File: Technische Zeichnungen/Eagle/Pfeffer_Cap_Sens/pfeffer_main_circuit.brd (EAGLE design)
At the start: 38 x 50 mm, 20 parts

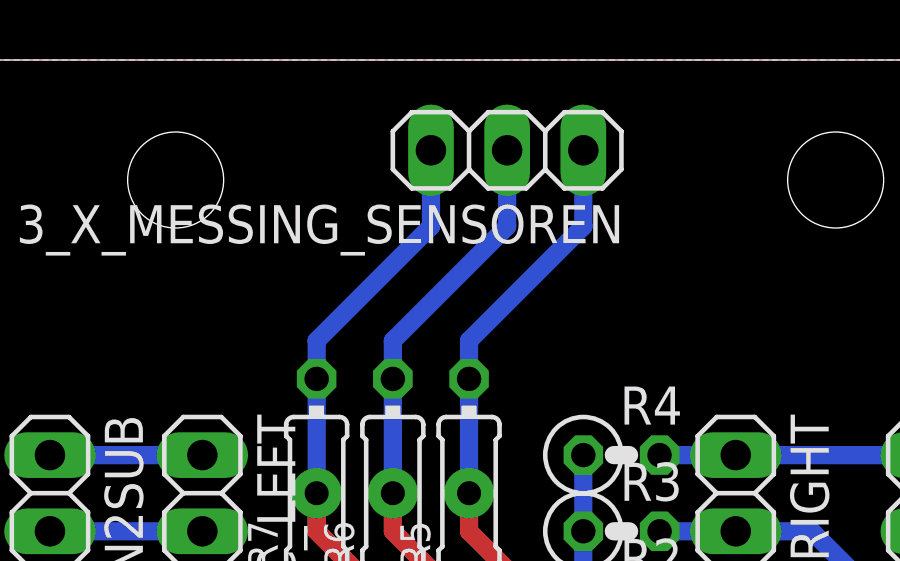
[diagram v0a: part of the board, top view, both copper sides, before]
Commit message: added ribbon testing, firmware and applied it to the new firmware, added a new tech. drawing, added new PCB layouts
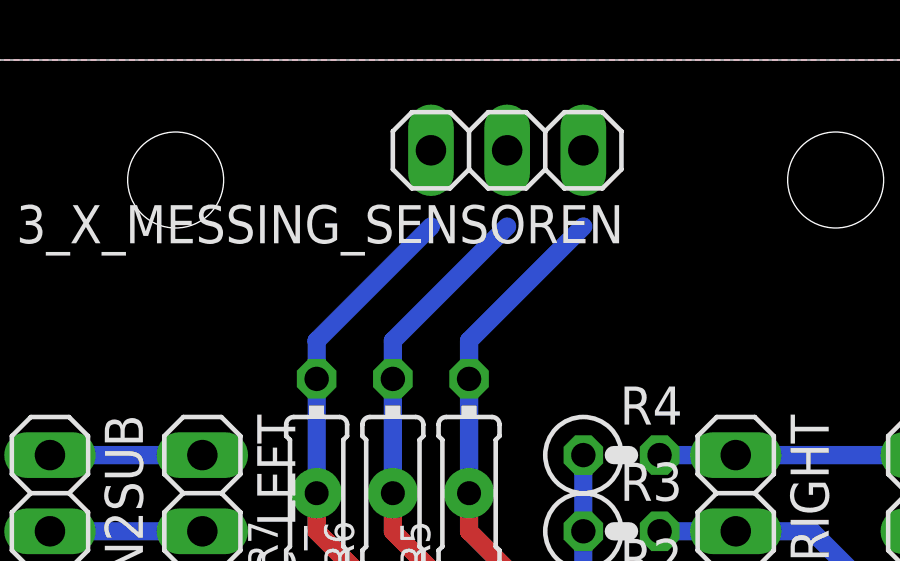
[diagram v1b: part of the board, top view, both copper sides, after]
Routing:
- net N$9: track 56.5 -> 54.0 mm
- net N$11: track 41.3 -> 38.7 mm
- net N$10: track 48.9 -> 46.3 mm
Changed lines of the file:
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@@
 <signal name="N$9">
 <contactref element="R5" pad="2"/>
-<contactref element="3_X_MESSING_SENSOREN" pad="1"/>
 <contactref element="R10" pad="1"/>
 <via x="21.59" y="24.13" extent="1-16" drill="0.8" diameter="1.6764" shape="octagon"/>
@@
 <wire x1="21.59" y1="25.4" x2="21.59" y2="24.13" width="0.6096" layer="1"/>
 <wire x1="17.78" y1="39.37" x2="17.78" y2="40.64" width="0.6096" layer="16"/>
-<wire x1="17.78" y1="40.64" x2="21.59" y2="44.45" width="0.6096" layer="16"/>
-<wire x1="21.59" y1="44.45" x2="21.59" y2="46.99" width="0.6096" layer="16"/>
+<wire x1="21.59" y1="44.45" x2="17.78" y2="40.64" width="0.6096" layer="16"/>
+<contactref element="3_X_MESSING_SENSOREN" pad="1"/>
+<wire x1="21.59" y1="44.45" x2="21.59" y2="46.99" width="0" layer="19" extent="16-16"/>
 </signal>
 <signal name="N$10">
 <contactref element="R6" pad="2"/>
-<contactref element="3_X_MESSING_SENSOREN" pad="2"/>
 <contactref element="R9" pad="1"/>
 <via x="19.05" y="21.59" extent="1-16" drill="0.8" diameter="1.6764" shape="octagon"/>
@@
 <wire x1="15.24" y1="35.56" x2="15.24" y2="39.37" width="0.6096" layer="16"/>
 <wire x1="15.24" y1="39.37" x2="15.24" y2="40.64" width="0.6096" layer="16"/>
-<wire x1="15.24" y1="40.64" x2="19.05" y2="44.45" width="0.6096" layer="16"/>
-<wire x1="19.05" y1="44.45" x2="19.05" y2="46.99" width="0.6096" layer="16"/>
+<wire x1="19.05" y1="44.45" x2="15.24" y2="40.64" width="0.6096" layer="16"/>
+<contactref element="3_X_MESSING_SENSOREN" pad="2"/>
+<wire x1="19.05" y1="44.45" x2="19.05" y2="46.99" width="0" layer="19" extent="16-16"/>
 </signal>
 <signal name="N$11">
 <contactref element="R7" pad="2"/>
-<contactref element="3_X_MESSING_SENSOREN" pad="3"/>
 <contactref element="R8" pad="1"/>
 <via x="16.51" y="19.05" extent="1-16" drill="0.8" diameter="1.6764" shape="octagon"/>
@@
 <wire x1="16.51" y1="25.4" x2="16.51" y2="19.05" width="0.6096" layer="1"/>
 <wire x1="12.7" y1="39.37" x2="12.7" y2="40.64" width="0.6096" layer="16"/>
-<wire x1="12.7" y1="40.64" x2="16.51" y2="44.45" width="0.6096" layer="16"/>
-<wire x1="16.51" y1="44.45" x2="16.51" y2="46.99" width="0.6096" layer="16"/>
+<wire x1="16.51" y1="44.45" x2="12.7" y2="40.64" width="0.6096" layer="16"/>
+<contactref element="3_X_MESSING_SENSOREN" pad="3"/>
+<wire x1="16.51" y1="44.45" x2="16.51" y2="46.99" width="0" layer="19" extent="16-16"/>
 </signal>
 <signal name="N$13">
